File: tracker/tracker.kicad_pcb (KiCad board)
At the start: 2 copper layers, 69 x 51.6 mm, 26 parts, among them J1 USB_C_Receptacle_PowerOnly_6P, Q1 DMG9926UDM-7, U1 XIAO-ESP32-C6-SMD, U2 LIS3DH, U3 DW01A, U4 INA226AIDGSR, U5 TP4056-42-ESOP8

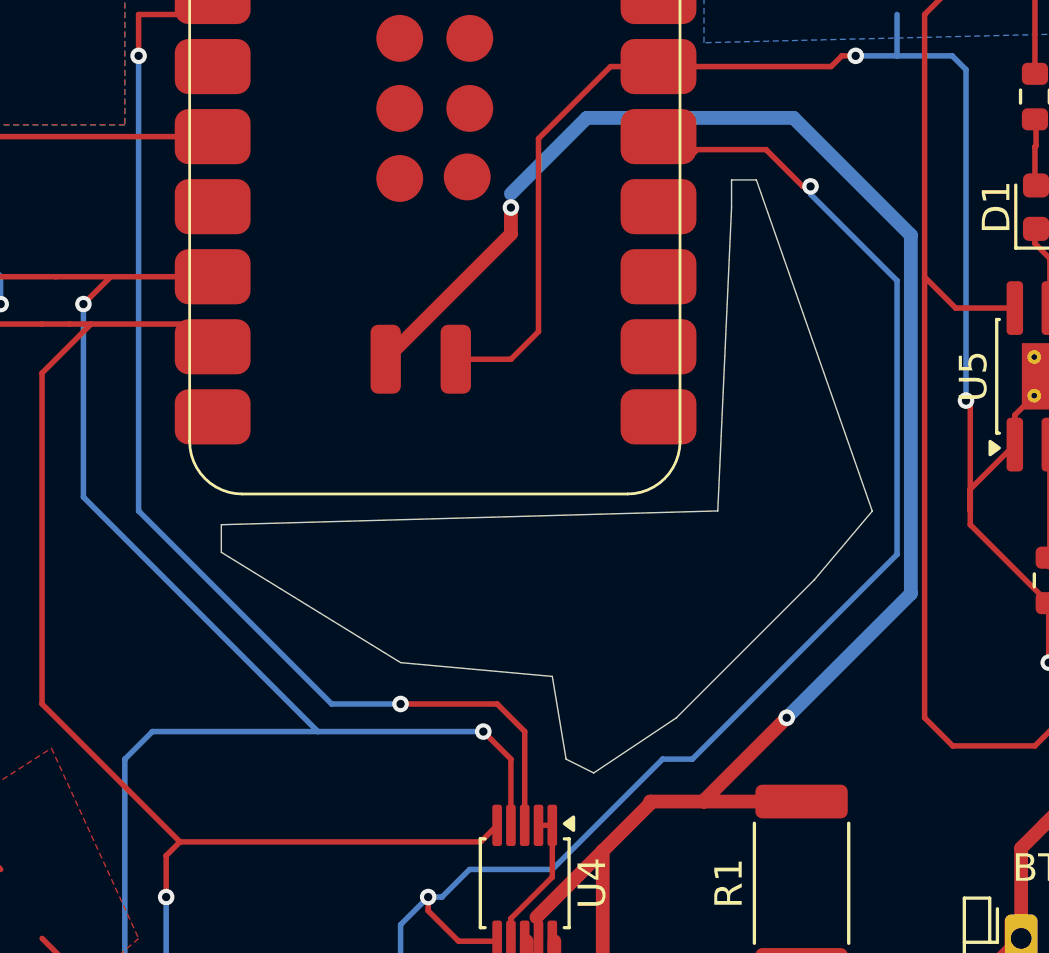
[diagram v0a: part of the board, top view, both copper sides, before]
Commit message: started v2 , placement sure routing is being done
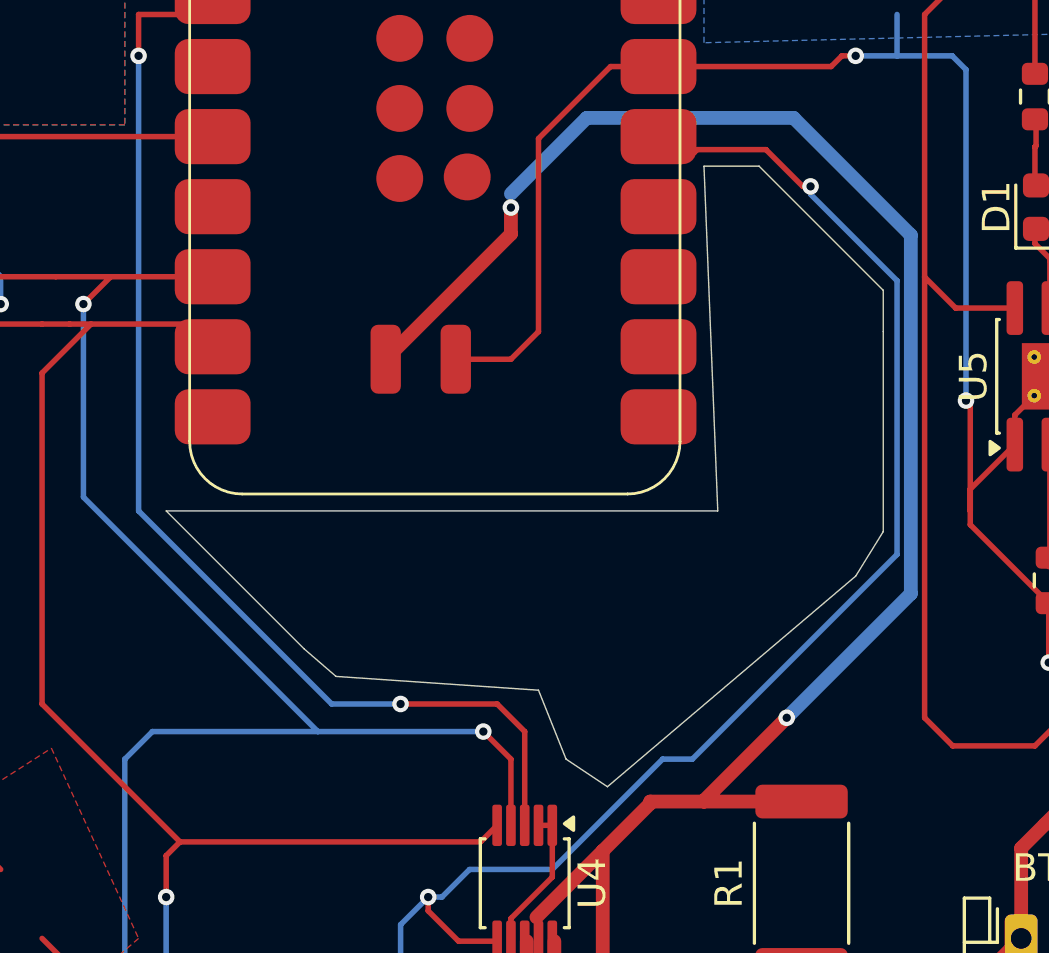
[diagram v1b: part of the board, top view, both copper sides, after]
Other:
- outline, holes or cut-outs redrawn
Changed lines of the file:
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@@
 	(gr_poly
 		(pts
-			(xy 131.899999 88) (xy 136.102358 100.006738) (xy 134 102.5) (xy 129 107.5) (xy 126 109.5) (xy 125 109)
-			(xy 124.5 106) (xy 119 105.5) (xy 112.5 101.5) (xy 112.5 100.5) (xy 130.5 100) (xy 131 89) (xy 131 88)
+			(xy 136.5 92) (xy 136.5 93.5) (xy 136.5 100.75) (xy 135.5 102.364108) (xy 126.5 110) (xy 125 109)
+			(xy 124 106.5) (xy 116.658889 106) (xy 115.5 105) (xy 110.5 100) (xy 130.5 100) (xy 130 87.5) (xy 132 87.5)
 		)
 		(stroke
